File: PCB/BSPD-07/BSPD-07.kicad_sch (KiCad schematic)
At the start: 54 parts, among them IC1 LM393LVQDRQ1, IC2 LM393LVQDRQ1, IC3 LM393LVQDRQ1, IC4 LDO40LPU50RY, IC5 74LVC1G02GW-Q100H, J1 DTM13-12PA, Q1 RSQ025P03HZGTR, Q2 RJU002N06FRAT106, Q3 RJU002N06FRAT106, U2 TLP175A / COMUS AB38-Q

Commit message: Almost finished schematics
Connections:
- net at IC3.1 (OUT1), R16.1: now also R17.1
- net 10s REF: now reaches IC3.5 (IN2+), R25.2, R26.1
- net 10ms VAL: now reaches C5.2, IC3.6 (IN2-), Q2.3, R14.2, R15.1
- net at Q1.3 (GATE), R16.2: no longer R17.1
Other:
- moved on the sheet: R16, R25, R26
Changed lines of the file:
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@@
   (junction (at 89.535 95.25) (diameter 0) (color 0 0 0 0)
   )
-  (junction (at 193.675 64.135) (diameter 0) (color 0 0 0 0)
+  (junction (at 193.675 68.58) (diameter 0) (color 0 0 0 0)
   )
   (junction (at 89.535 35.56) (diameter 0) (color 0 0 0 0)
@@
   (junction (at 36.83 100.33) (diameter 0) (color 0 0 0 0)
   )
+  (junction (at 215.9 42.545) (diameter 0) (color 0 0 0 0)
+  )
   (junction (at 90.17 41.91) (diameter 0) (color 0 0 0 0)
   )
   (junction (at 220.98 120.65) (diameter 0) (color 0 0 0 0)
-  )
-  (junction (at 218.44 42.545) (diameter 0) (color 0 0 0 0)
   )
   (junction (at 220.98 123.19) (diameter 0) (color 0 0 0 0)
@@
     (stroke (width 0) (type default) (color 0 0 0 0))
   )
-  (wire (pts (xy 218.44 42.545) (xy 218.44 48.26))
-    (stroke (width 0) (type default) (color 0 0 0 0))
-  )
   (wire (pts (xy 173.99 38.735) (xy 175.895 38.735))
     (stroke (width 0) (type default) (color 0 0 0 0))
@@
     (stroke (width 0) (type default) (color 0 0 0 0))
   )
+  (wire (pts (xy 218.44 48.26) (xy 218.44 44.45))
+    (stroke (width 0) (type default) (color 0 0 0 0))
+  )
   (wire (pts (xy 262.255 62.23) (xy 262.255 64.135))
     (stroke (width 0) (type default) (color 0 0 0 0))
@@
     (stroke (width 0) (type default) (color 0 0 0 0))
   )
-  (wire (pts (xy 193.675 62.865) (xy 193.675 64.135))
+  (wire (pts (xy 193.675 62.865) (xy 193.675 68.58))
     (stroke (width 0) (type default) (color 0 0 0 0))
   )
@@
     (stroke (width 0) (type default) (color 0 0 0 0))
   )
-  (wire (pts (xy 191.77 64.135) (xy 193.675 64.135))
+  (wire (pts (xy 191.77 68.58) (xy 193.675 68.58))
     (stroke (width 0) (type default) (color 0 0 0 0))
   )
@@
     (stroke (width 0) (type default) (color 0 0 0 0))
   )
+  (wire (pts (xy 215.9 44.45) (xy 215.9 42.545))
+    (stroke (width 0) (type default) (color 0 0 0 0))
+  )
   (wire (pts (xy 34.925 40.64) (xy 36.83 40.64))
     (stroke (width 0) (type default) (color 0 0 0 0))
@@
     (stroke (width 0) (type default) (color 0 0 0 0))
   )
-  (wire (pts (xy 193.675 69.85) (xy 193.675 71.12))
+  (wire (pts (xy 193.675 74.295) (xy 193.675 75.565))
     (stroke (width 0) (type default) (color 0 0 0 0))
   )
@@
     (stroke (width 0) (type default) (color 0 0 0 0))
   )
-  (wire (pts (xy 210.185 42.545) (xy 212.725 42.545))
-    (stroke (width 0) (type default) (color 0 0 0 0))
-  )
   (polyline (pts (xy 150.495 24.765) (xy 193.675 24.765))
     (stroke (width 0) (type default) (color 0 0 0 0))
@@
     (stroke (width 0) (type default) (color 0 0 0 0))
   )
-  (wire (pts (xy 193.675 64.135) (xy 193.675 64.77))
+  (wire (pts (xy 210.185 42.545) (xy 215.9 42.545))
+    (stroke (width 0) (type default) (color 0 0 0 0))
+  )
+  (wire (pts (xy 193.675 68.58) (xy 193.675 69.215))
     (stroke (width 0) (type default) (color 0 0 0 0))
   )
@@
     (stroke (width 0) (type default) (color 0 0 0 0))
   )
-  (wire (pts (xy 184.785 64.135) (xy 186.69 64.135))
+  (wire (pts (xy 184.785 68.58) (xy 186.69 68.58))
     (stroke (width 0) (type default) (color 0 0 0 0))
   )
@@
     (stroke (width 0) (type default) (color 0 0 0 0))
   )
-  (wire (pts (xy 217.805 42.545) (xy 218.44 42.545))
-    (stroke (width 0) (type default) (color 0 0 0 0))
-  )
   (wire (pts (xy 179.705 41.275) (xy 182.245 41.275))
     (stroke (width 0) (type default) (color 0 0 0 0))
@@
     (stroke (width 0) (type default) (color 0 0 0 0))
   )
-  (wire (pts (xy 218.44 42.545) (xy 220.98 42.545))
-    (stroke (width 0) (type default) (color 0 0 0 0))
-  )
   (wire (pts (xy 220.98 47.625) (xy 220.98 52.07))
     (stroke (width 0) (type default) (color 0 0 0 0))
   )
   (wire (pts (xy 166.37 186.055) (xy 168.275 186.055))
+    (stroke (width 0) (type default) (color 0 0 0 0))
+  )
+  (wire (pts (xy 218.44 44.45) (xy 215.9 44.45))
     (stroke (width 0) (type default) (color 0 0 0 0))
   )
@@
   (text "BSPD for PGR-07 (2023)" (at 186.69 191.135 0)
     (effects (font (size 1.6 1.6) (thickness 0.32) bold italic) (justify left bottom))
+  )
+  (label "10ms VAL" (at 222.25 67.31 0)
+    (effects (font (size 1.27 1.27)) (justify left bottom))
+  )
+  (label "10s REF" (at 193.675 67.31 90)
+    (effects (font (size 1.27 1.27)) (justify left bottom))
   )
   (label "500MS_REF" (at 177.165 38.735 0)
@@
     (pin "1")
   )
-  (symbol (lib_id "power:GND") (at 193.675 71.12 0) (unit 1)
-    (in_bom yes) (on_board yes) (fields_autoplaced)
-    (property "Reference" "#PWR0149" (id 0) (at 193.675 77.47 0)
-      (effects (font (size 1.27 1.27)) hide)
-    )
-    (property "Value" "GND" (id 1) (at 193.675 76.2 0))
-    (property "Footprint" "" (id 2) (at 193.675 71.12 0)
-      (effects (font (size 1.27 1.27)) hide)
-    )
-    (property "Datasheet" "" (id 3) (at 193.675 71.12 0)
+  (symbol (lib_id "power:GND") (at 193.675 75.565 0) (unit 1)
+    (in_bom yes) (on_board yes) (fields_autoplaced)
+    (property "Reference" "#PWR0149" (id 0) (at 193.675 81.915 0)
+      (effects (font (size 1.27 1.27)) hide)
+    )
+    (property "Value" "GND" (id 1) (at 193.675 80.645 0))
+    (property "Footprint" "" (id 2) (at 193.675 75.565 0)
+      (effects (font (size 1.27 1.27)) hide)
+    )
+    (property "Datasheet" "" (id 3) (at 193.675 75.565 0)
       (effects (font (size 1.27 1.27)) hide)
     )
@@
     (pin "2")
   )
-  (symbol (lib_id "power:+5V") (at 184.785 64.135 90) (unit 1)
-    (in_bom yes) (on_board yes) (fields_autoplaced)
-    (property "Reference" "#PWR0148" (id 0) (at 188.595 64.135 0)
-      (effects (font (size 1.27 1.27)) hide)
-    )
-    (property "Value" "+5V" (id 1) (at 181.61 64.1349 90)
-      (effects (font (size 1.27 1.27)) (justify left))
-    )
-    (property "Footprint" "" (id 2) (at 184.785 64.135 0)
-      (effects (font (size 1.27 1.27)) hide)
-    )
-    (property "Datasheet" "" (id 3) (at 184.785 64.135 0)
+  (symbol (lib_id "power:+5V") (at 184.785 68.58 90) (unit 1)
+    (in_bom yes) (on_board yes) (fields_autoplaced)
+    (property "Reference" "#PWR0148" (id 0) (at 188.595 68.58 0)
+      (effects (font (size 1.27 1.27)) hide)
+    )
+    (property "Value" "+5V" (id 1) (at 181.61 68.5799 90)
+      (effects (font (size 1.27 1.27)) (justify left))
+    )
+    (property "Footprint" "" (id 2) (at 184.785 68.58 0)
+      (effects (font (size 1.27 1.27)) hide)
+    )
+    (property "Datasheet" "" (id 3) (at 184.785 68.58 0)
       (effects (font (size 1.27 1.27)) hide)
     )
@@
     (pin "8")
   )
-  (symbol (lib_id "Device:R_Small") (at 189.23 64.135 90) (unit 1)
-    (in_bom yes) (on_board yes)
-    (property "Reference" "R25" (id 0) (at 189.23 60.325 90))
-    (property "Value" "39k" (id 1) (at 189.23 62.23 90))
-    (property "Footprint" "Resistor_SMD:R_0402_1005Metric" (id 2) (at 189.23 64.135 0)
-      (effects (font (size 1.27 1.27)) hide)
-    )
-    (property "Datasheet" "~" (id 3) (at 189.23 64.135 0)
+  (symbol (lib_id "Device:R_Small") (at 189.23 68.58 90) (unit 1)
+    (in_bom yes) (on_board yes)
+    (property "Reference" "R25" (id 0) (at 189.23 64.77 90))
+    (property "Value" "39k" (id 1) (at 189.23 66.675 90))
+    (property "Footprint" "Resistor_SMD:R_0402_1005Metric" (id 2) (at 189.23 68.58 0)
+      (effects (font (size 1.27 1.27)) hide)
+    )
+    (property "Datasheet" "~" (id 3) (at 189.23 68.58 0)
       (effects (font (size 1.27 1.27)) hide)
     )
@@
     (pin "1")
   )
-  (symbol (lib_id "Device:R_Small") (at 215.265 42.545 90) (unit 1)
-    (in_bom yes) (on_board yes)
-    (property "Reference" "R16" (id 0) (at 213.995 40.64 90)
+  (symbol (lib_id "Device:R_Small") (at 218.44 42.545 90) (unit 1)
+    (in_bom yes) (on_board yes)
+    (property "Reference" "R16" (id 0) (at 217.17 40.64 90)
       (effects (font (size 0.8 0.8)))
     )
-    (property "Value" "100" (id 1) (at 216.535 40.64 90)
+    (property "Value" "100" (id 1) (at 219.71 40.64 90)
       (effects (font (size 0.8 0.8)))
     )
-    (property "Footprint" "Resistor_SMD:R_0402_1005Metric" (id 2) (at 215.265 42.545 0)
-      (effects (font (size 1.27 1.27)) hide)
-    )
-    (property "Datasheet" "~" (id 3) (at 215.265 42.545 0)
+    (property "Footprint" "Resistor_SMD:R_0402_1005Metric" (id 2) (at 218.44 42.545 0)
+      (effects (font (size 1.27 1.27)) hide)
+    )
+    (property "Datasheet" "~" (id 3) (at 218.44 42.545 0)
       (effects (font (size 1.27 1.27)) hide)
     )
@@
     (pin "1")
   )
-  (symbol (lib_id "Device:R_Small") (at 193.675 67.31 0) (unit 1)
-    (in_bom yes) (on_board yes) (fields_autoplaced)
-    (property "Reference" "R26" (id 0) (at 195.58 66.0399 0)
-      (effects (font (size 1.27 1.27)) (justify left))
-    )
-    (property "Value" "10k" (id 1) (at 195.58 68.5799 0)
-      (effects (font (size 1.27 1.27)) (justify left))
-    )
-    (property "Footprint" "Resistor_SMD:R_0402_1005Metric" (id 2) (at 193.675 67.31 0)
-      (effects (font (size 1.27 1.27)) hide)
-    )
-    (property "Datasheet" "~" (id 3) (at 193.675 67.31 0)
-      (effects (font (size 1.27 1.27)) hide)
-    )
+  (symbol (lib_id "Device:R_Small") (at 193.675 71.755 0) (unit 1)
+    (in_bom yes) (on_board yes) (fields_autoplaced)
+    (property "Reference" "R26" (id 0) (at 195.58 70.4849 0)
+      (effects (font (size 1.27 1.27)) (justify left))
+    )
+    (property "Value" "10k" (id 1) (at 195.58 73.0249 0)
+      (effects (font (size 1.27 1.27)) (justify left))
+    )
+    (property "Footprint" "Resistor_SMD:R_0402_1005Metric" (id 2) (at 193.675 71.755 0)
+      (effects (font (size 1.27 1.27)) hide)
+    )
+    (property "Datasheet" "~" (id 3) (at 193.675 71.755 0)
+      (effects (font (size 1.27 1.27)) hide)
+    )

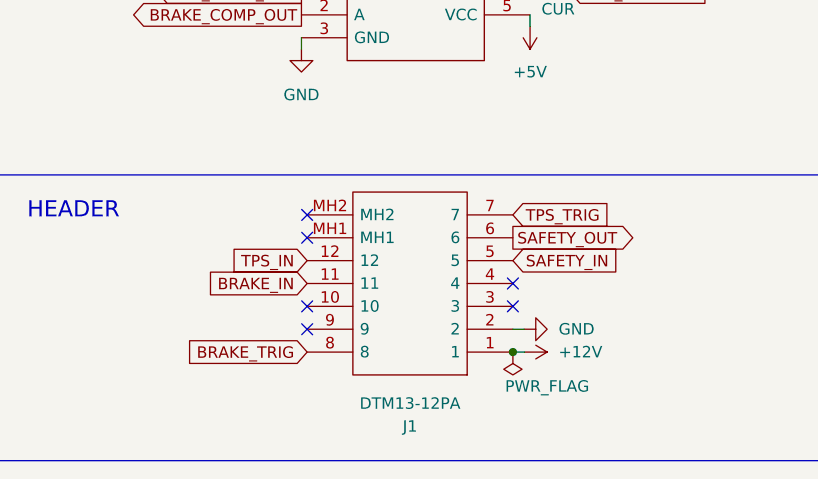
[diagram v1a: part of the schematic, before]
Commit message: Finished PCB layout
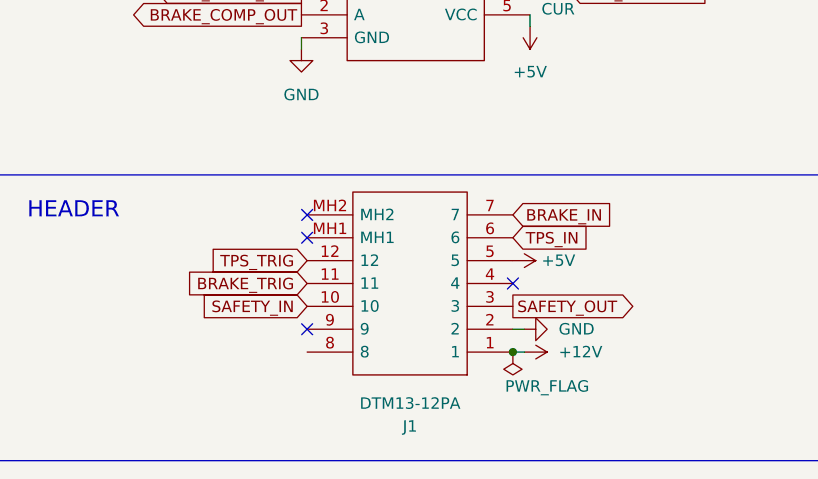
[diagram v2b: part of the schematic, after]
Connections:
- net +5V: now also J1.5
- net BRAKE_IN: now also J1.7; no longer J1.11
- net BRAKE_TRIG: now also J1.11; no longer J1.8
- net SAFETY_IN: now also J1.10; no longer J1.5
- net SAFETY_OUT: now also J1.3; no longer J1.6
- net TPS_IN: now also J1.6; no longer J1.12
- net TPS_TRIG: now also J1.12; no longer J1.7
- no-connect marks 9 -> 7
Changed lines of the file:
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@@
   (no_connect (at 50.8 87.63))
   (no_connect (at 50.165 170.815))
-  (no_connect (at 50.165 180.975))
   (no_connect (at 50.165 183.515))
   (no_connect (at 50.165 173.355))
   (no_connect (at 73.025 178.435))
   (no_connect (at 50.8 27.94))
-  (no_connect (at 73.025 180.975))
   (no_connect (at 261.62 118.11))
   (wire (pts (xy 74.93 146.05) (xy 76.835 146.05))
@@
     )
   )
-  (global_label "BRAKE_IN" (shape input) (at 50.165 178.435 180) (fields_autoplaced)
-    (effects (font (size 1.27 1.27)) (justify right))
-    (property "Intersheet References" "${INTERSHEET_REFS}" (id 0) (at 38.8014 178.3556 0)
-      (effects (font (size 1.27 1.27)) (justify right) hide)
+  (global_label "BRAKE_IN" (shape input) (at 73.025 170.815 0) (fields_autoplaced)
+    (effects (font (size 1.27 1.27)) (justify left))
+    (property "Intersheet References" "${INTERSHEET_REFS}" (id 0) (at 84.3886 170.8944 0)
+      (effects (font (size 1.27 1.27)) (justify left) hide)
     )
   )
@@
     )
   )
-  (global_label "TPS_TRIG" (shape input) (at 73.025 170.815 0) (fields_autoplaced)
-    (effects (font (size 1.27 1.27)) (justify left))
-    (property "Intersheet References" "${INTERSHEET_REFS}" (id 0) (at 83.9652 170.7356 0)
-      (effects (font (size 1.27 1.27)) (justify left) hide)
+  (global_label "TPS_TRIG" (shape input) (at 50.165 175.895 180) (fields_autoplaced)
+    (effects (font (size 1.27 1.27)) (justify right))
+    (property "Intersheet References" "${INTERSHEET_REFS}" (id 0) (at 39.2248 175.9744 0)
+      (effects (font (size 1.27 1.27)) (justify right) hide)
     )
   )
@@
     )
   )
-  (global_label "TPS_IN" (shape input) (at 50.165 175.895 180) (fields_autoplaced)
-    (effects (font (size 1.27 1.27)) (justify right))
-    (property "Intersheet References" "${INTERSHEET_REFS}" (id 0) (at 41.4019 175.9744 0)
-      (effects (font (size 1.27 1.27)) (justify right) hide)
+  (global_label "TPS_IN" (shape input) (at 73.025 173.355 0) (fields_autoplaced)
+    (effects (font (size 1.27 1.27)) (justify left))
+    (property "Intersheet References" "${INTERSHEET_REFS}" (id 0) (at 81.7881 173.2756 0)
+      (effects (font (size 1.27 1.27)) (justify left) hide)
     )
   )
@@
     )
   )
-  (global_label "BRAKE_TRIG" (shape input) (at 50.165 186.055 180) (fields_autoplaced)
+  (global_label "BRAKE_TRIG" (shape input) (at 50.165 178.435 180) (fields_autoplaced)
     (effects (font (size 1.27 1.27)) (justify right))
-    (property "Intersheet References" "${INTERSHEET_REFS}" (id 0) (at 36.6243 186.1344 0)
+    (property "Intersheet References" "${INTERSHEET_REFS}" (id 0) (at 36.6243 178.5144 0)
       (effects (font (size 1.27 1.27)) (justify right) hide)
     )
   )
-  (global_label "SAFETY_IN" (shape input) (at 73.025 175.895 0) (fields_autoplaced)
-    (effects (font (size 1.27 1.27)) (justify left))
-    (property "Intersheet References" "${INTERSHEET_REFS}" (id 0) (at 84.9329 175.8156 0)
-      (effects (font (size 1.27 1.27)) (justify left) hide)
+  (global_label "SAFETY_IN" (shape input) (at 50.165 180.975 180) (fields_autoplaced)
+    (effects (font (size 1.27 1.27)) (justify right))
+    (property "Intersheet References" "${INTERSHEET_REFS}" (id 0) (at 38.2571 181.0544 0)
+      (effects (font (size 1.27 1.27)) (justify right) hide)
     )
   )
@@
     )
   )
-  (global_label "SAFETY_OUT" (shape output) (at 73.025 173.355 0) (fields_autoplaced)
+  (global_label "SAFETY_OUT" (shape output) (at 73.025 180.975 0) (fields_autoplaced)
     (effects (font (size 1.27 1.27)) (justify left))
-    (property "Intersheet References" "${INTERSHEET_REFS}" (id 0) (at 86.6262 173.2756 0)
+    (property "Intersheet References" "${INTERSHEET_REFS}" (id 0) (at 86.6262 180.8956 0)
       (effects (font (size 1.27 1.27)) (justify left) hide)
     )
@@
     (pin "1")
   )
+  (symbol (lib_id "power:+5V") (at 73.025 175.895 270) (unit 1)
+    (in_bom yes) (on_board yes) (fields_autoplaced)
+    (property "Reference" "#PWR0150" (id 0) (at 69.215 175.895 0)
+      (effects (font (size 1.27 1.27)) hide)
+    )
+    (property "Value" "+5V" (id 1) (at 76.2 175.8949 90)
+      (effects (font (size 1.27 1.27)) (justify left))
+    )
+    (property "Footprint" "" (id 2) (at 73.025 175.895 0)
+      (effects (font (size 1.27 1.27)) hide)
+    )
+    (property "Datasheet" "" (id 3) (at 73.025 175.895 0)
+      (effects (font (size 1.27 1.27)) hide)
+    )
+    (pin "1")
+  )
   (symbol (lib_id "power:+5V") (at 90.17 113.03 180) (unit 1)
     (in_bom yes) (on_board yes) (fields_autoplaced)
@@
       (reference "#PWR0149") (unit 1) (value "GND") (footprint "")
     )
+    (path "/c6610192-8889-4eb3-a28b-ca4e583728d5"
+      (reference "#PWR0150") (unit 1) (value "+5V") (footprint "")
+    )
     (path "/118f0778-e9d3-4271-8bcc-a274169adaa4"

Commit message: Tinkle of a rose petal ;)
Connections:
- no-connect marks 7 -> 8
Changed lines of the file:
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@@
   (no_connect (at 50.165 173.355))
   (no_connect (at 73.025 178.435))
+  (no_connect (at 50.165 186.055))
   (no_connect (at 50.8 27.94))
   (no_connect (at 261.62 118.11))
